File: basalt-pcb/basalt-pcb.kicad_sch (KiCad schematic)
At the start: 10 parts, among them J1 Conn_01x06_Pin, J2 Conn_01x06_Pin, J3 USB4215-03-A, U1 DI78L3.3ZAB, U2 STM32C071F8Px

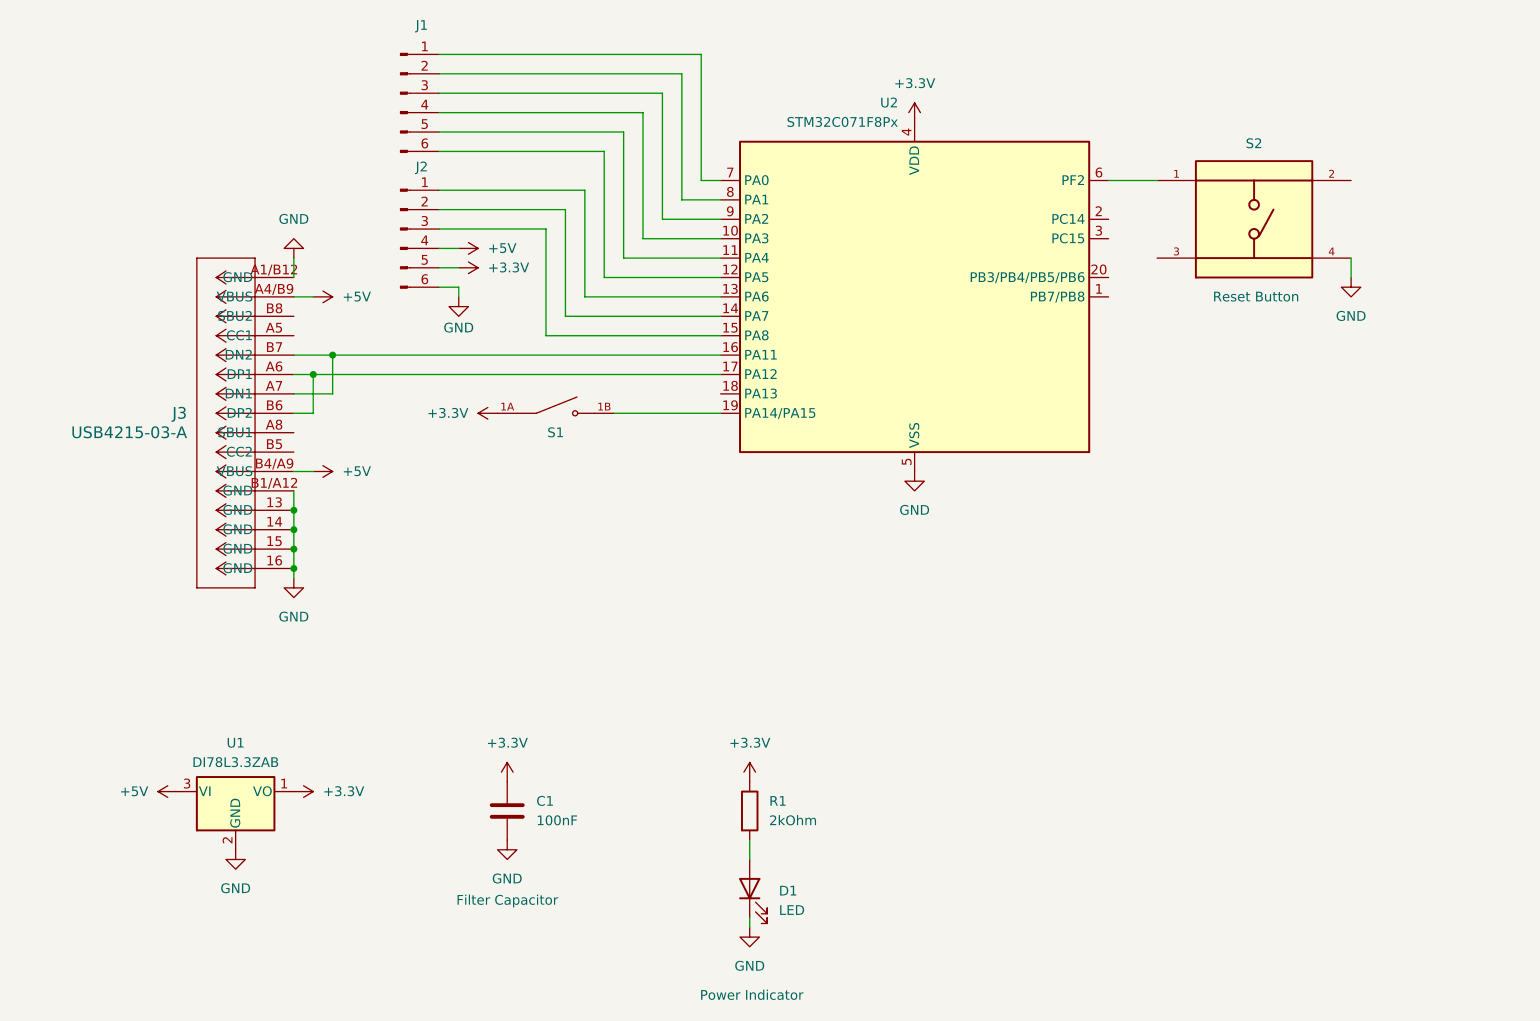
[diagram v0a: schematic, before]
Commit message: Expose more pins, add ST-link pins at back, add diode to prevent backfeeding USB port
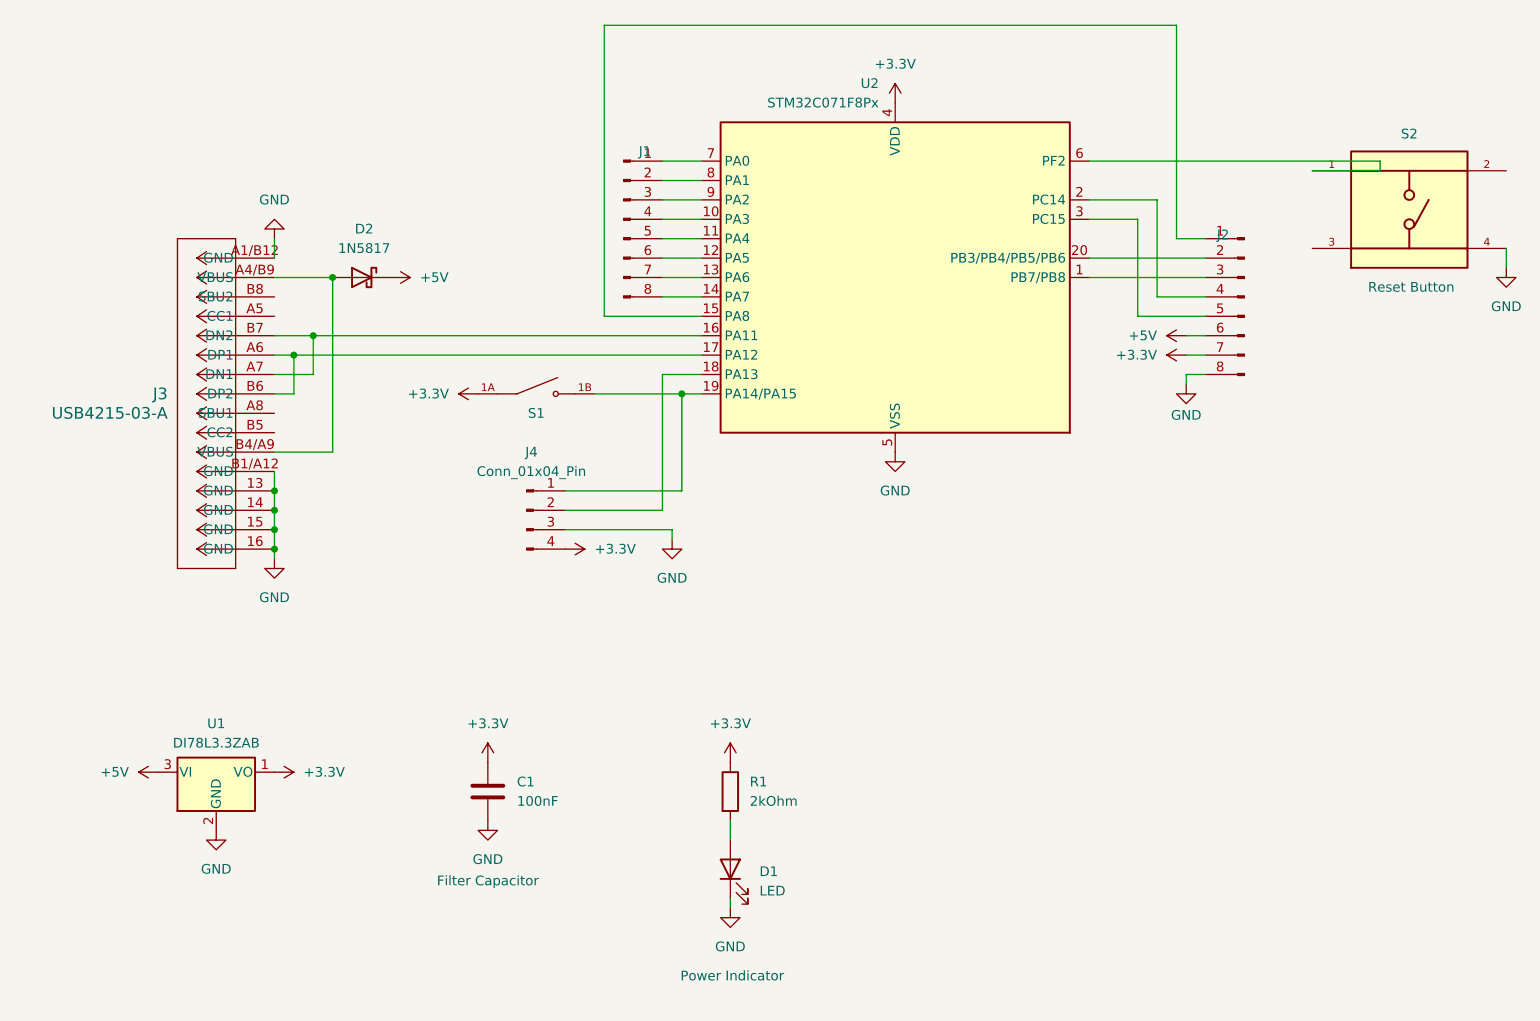
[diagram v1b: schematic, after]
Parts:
- added D2: 1N5817, Diode_THT:D_DO-41_SOD81_P10.16mm_Horizontal, symbol Diode:1N5817
- added J4: Conn_01x04_Pin, Connector_PinHeader_2.54mm:PinHeader_1x04_P2.54mm_Vertical, symbol Connector:Conn_01x04_Pin
- J1, J2: value Conn_01x06_Pin -> Conn_01x08_Pin; footprint Connector_PinHeader_2.54mm:PinHeader_1x06_P2.54mm_Vertical -> Connector_PinHeader_2.54mm:PinHeader_1x08_P2.54mm_Vertical; symbol Connector:Conn_01x06_Pin -> Connector:Conn_01x08_Pin
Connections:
- net +3.3V: now also J2.7 (Pin_7), J4.4 (Pin_4); no longer J2.5 (Pin_5)
- net +5V: now also J2.6 (Pin_6), D2.1 (K); no longer J2.4 (Pin_4), J3.A4/B9 (VBUS), J3.B4/A9 (VBUS)
- net GND: now also J2.8 (Pin_8), J4.3 (Pin_3); no longer J2.6 (Pin_6)
- net at U2.13 (PA6): now also J1.7 (Pin_7); no longer J2.1 (Pin_1)
- net at U2.14 (PA7): now also J1.8 (Pin_8); no longer J2.2 (Pin_2)
- net at U2.15 (PA8): now also J2.1 (Pin_1); no longer J2.3 (Pin_3)
- net at S1.1B, U2.19 (PA14/PA15): now also J4.1 (Pin_1)
- net at U2.1 (PB7/PB8): now also J2.3 (Pin_3)
- net at U2.18 (PA13): now also J4.2 (Pin_2)
- net at U2.2 (PC14): now also J2.4 (Pin_4)
- net at U2.20 (PB3/PB4/PB5/PB6): now also J2.2 (Pin_2)
- net at U2.3 (PC15): now also J2.5 (Pin_5)
- new net: D2.2 (A), J3.A4/B9 (VBUS), J3.B4/A9 (VBUS)
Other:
- moved on the sheet: C1, D1, J3, R1, S1, S2, U1, U2
